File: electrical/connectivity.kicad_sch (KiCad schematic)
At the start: 0 parts

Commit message: #3 Adding controls connections to STM32, updating IOC file to match.
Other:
- company: (none) -> AlumaPower
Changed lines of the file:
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@@
 	(generator_version "9.0")
 	(paper "A4")
+	(title_block
+		(company "AlumaPower")
+	)
 	(bus_entry
 		(at 49.53 68.58)

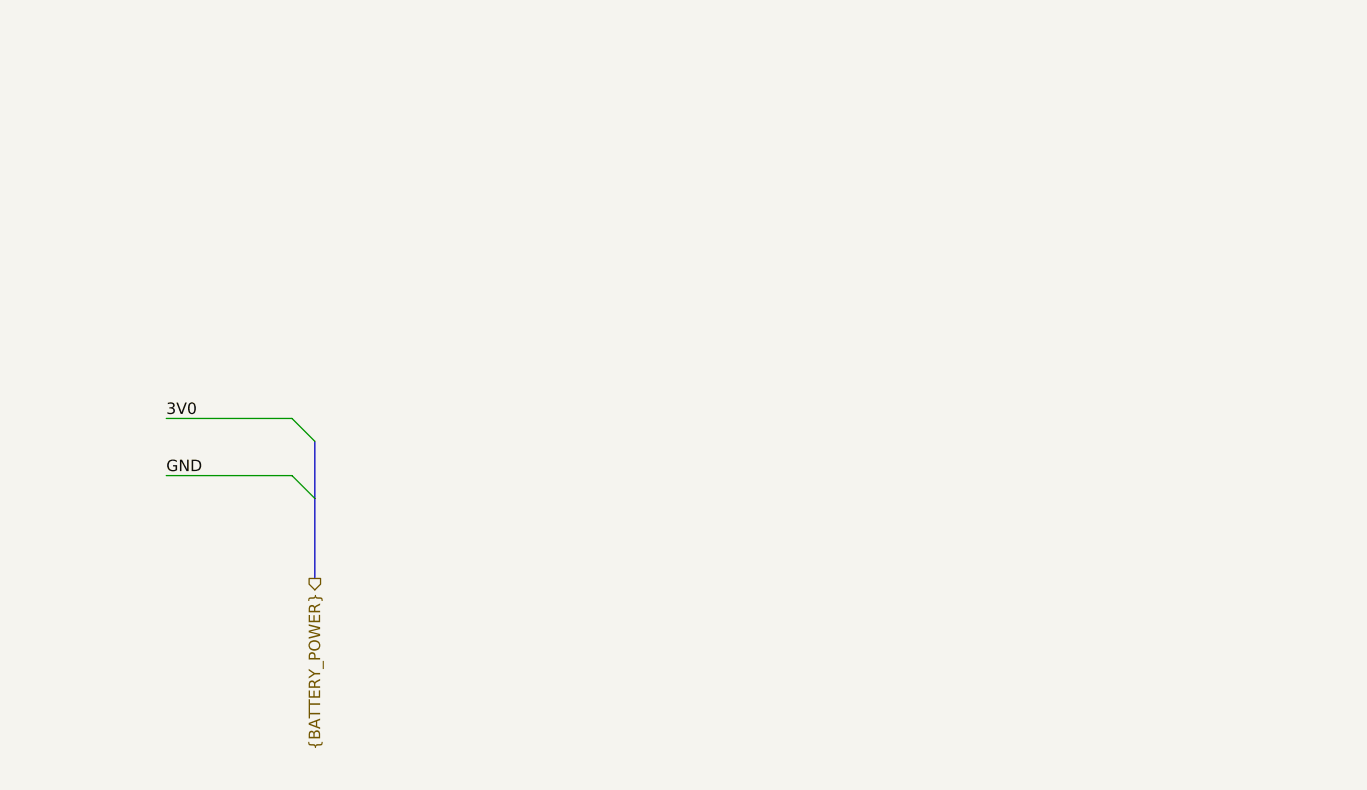
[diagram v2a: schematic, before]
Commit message: #3 Adding WiFi module to the schematic.
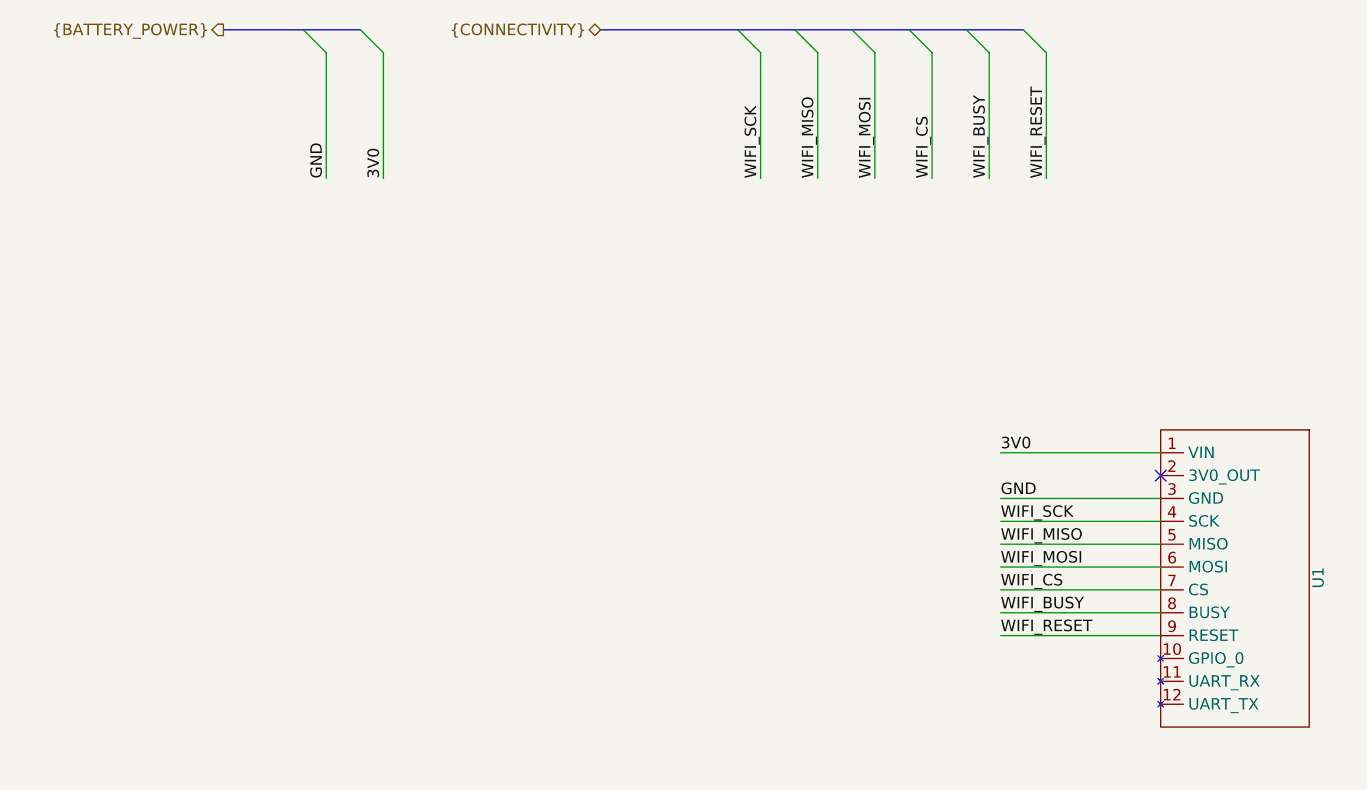
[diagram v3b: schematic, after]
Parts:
- added U1: ~, custom:esp32_wifi_module, symbol custom:wifi_module
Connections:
- net 3V0: now also U1.1 (VIN)
- net GND: now also U1.3 (GND)
- new net WIFI_BUSY: U1.8 (BUSY)
- new net WIFI_CS: U1.7 (CS)
- new net WIFI_MISO: U1.5 (MISO)
- new net WIFI_MOSI: U1.6 (MOSI)
- new net WIFI_RESET: U1.9 (RESET)
- new net WIFI_SCK: U1.4 (SCK)
- no-connect marks 0 -> 1
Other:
- title: (none) -> Etchasketch - Connectivity

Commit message: #17 Making layout. Errors rpesent.
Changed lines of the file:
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@@
 		(company "AlumaPower")
+	)
+	(bus_alias "BATTERY_POWER"
+		(members "3V0" "GND")
+	)
+	(bus_alias "CONNECTIVITY"
+		(members "WIFI_SCK" "WIFI_MISO" "WIFI_MOSI" "WIFI_CS" "WIFI_BUSY" "WIFI_RESET")
+	)
+	(bus_alias "SCREEN_INTERFACE"
+		(members "SCREEN_SDA" "SCREEN_SCL" "SCREEN_CS" "SCREEN_D_C" "SCREEN_RST"
+			"SCREEN_BUSY"
+		)
 	)
 	(no_connect
@@
 	)
 	(bus_entry
-		(at 54.61 29.21)
-		(size -2.54 -2.54)
-		(stroke
-			(width 0)
-			(type default)
-		)
-	)
-	(bus_entry
 		(at 111.76 25.4)
 		(size 2.54 2.54)
@@
 	)
 	(bus_entry
-		(at 60.96 29.21)
-		(size -2.54 -2.54)
+		(at 43.18 25.4)
+		(size 2.54 2.54)
+		(stroke
+			(width 0)
+			(type default)
+		)
+	)
+	(bus_entry
+		(at 48.26 25.4)
+		(size 2.54 2.54)
+		(stroke
+			(width 0)
+			(type default)
+		)
+	)
+	(wire
+		(pts
+			(xy 50.8 27.94) (xy 50.8 35.56)
+		)
 		(stroke
 			(width 0)
@@
 		)
 	)
+	(wire
+		(pts
+			(xy 45.72 27.94) (xy 45.72 35.56)
+		)
+		(stroke
+			(width 0)
+			(type default)
+		)
+	)
 	(bus
 		(pts
@@
 	(wire
 		(pts
-			(xy 54.61 43.18) (xy 54.61 29.21)
-		)
-		(stroke
-			(width 0)
-			(type default)
-		)
-	)
-	(wire
-		(pts
 			(xy 128.27 92.71) (xy 146.05 92.71)
 		)
@@
 	(wire
 		(pts
+			(xy 102.87 72.39) (xy 120.65 72.39)
+		)
+		(stroke
+			(width 0)
+			(type default)
+		)
+	)
+	(wire
+		(pts
 			(xy 128.27 90.17) (xy 146.05 90.17)
 		)
@@
 		)
 	)
+	(bus
+		(pts
+			(xy 40.64 25.4) (xy 43.18 25.4)
+		)
+		(stroke
+			(width 0)
+			(type default)
+		)
+	)
 	(wire
 		(pts
@@
 	(bus
 		(pts
-			(xy 52.07 26.67) (xy 43.18 26.67)
-		)
-		(stroke
-			(width 0)
-			(type default)
-		)
-	)
-	(wire
-		(pts
-			(xy 60.96 43.18) (xy 60.96 29.21)
-		)
-		(stroke
-			(width 0)
-			(type default)
-		)
-	)
-	(bus
-		(pts
 			(xy 99.06 25.4) (xy 105.41 25.4)
 		)
@@
 		)
 	)
+	(bus
+		(pts
+			(xy 43.18 25.4) (xy 48.26 25.4)
+		)
+		(stroke
+			(width 0)
+			(type default)
+		)
+	)
 	(wire
 		(pts
@@
 	(bus
 		(pts
-			(xy 58.42 26.67) (xy 52.07 26.67)
+			(xy 48.26 25.4) (xy 54.61 25.4)
 		)
 		(stroke
@@
 			(width 0)
 			(type default)
+		)
+	)
+	(label "GND"
+		(at 50.8 35.56 90)
+		(effects
+			(font
+				(size 1.27 1.27)
+			)
+			(justify left bottom)
 		)
 	)
@@
 		)
 	)
+	(label "VIN"
+		(at 120.65 72.39 180)
+		(effects
+			(font
+				(size 1.27 1.27)
+			)
+			(justify right bottom)
+		)
+	)
 	(label "WIFI_BUSY"
 		(at 120.65 41.91 90)
@@
 		)
 	)
+	(label "VIN"
+		(at 128.27 72.39 0)
+		(effects
+			(font
+				(size 1.27 1.27)
+			)
+			(justify left bottom)
+		)
+	)
 	(label "WIFI_CS"
 		(at 128.27 87.63 0)
@@
 		)
 	)
-	(label "3V0"
-		(at 128.27 72.39 0)
-		(effects
-			(font
-				(size 1.27 1.27)
-			)
-			(justify left bottom)
-		)
-	)
 	(label "WIFI_MOSI"
 		(at 128.27 85.09 0)
@@
 		)
 	)
+	(label "3V0"
+		(at 45.72 35.56 90)
+		(effects
+			(font
+				(size 1.27 1.27)
+			)
+			(justify left bottom)
+		)
+	)
 	(label "WIFI_MOSI"
 		(at 107.95 41.91 90)
@@
 		)
 	)
-	(label "3V0"
-		(at 60.96 43.18 90)
-		(effects
-			(font
-				(size 1.27 1.27)
-			)
-			(justify left bottom)
-		)
-	)
-	(label "GND"
-		(at 54.61 43.18 90)
-		(effects
-			(font
-				(size 1.27 1.27)
-			)
-			(justify left bottom)
-		)
-	)
 	(label "WIFI_CS"
 		(at 114.3 41.91 90)
@@
 		)
 	)
+	(label "3V0"
+		(at 102.87 72.39 0)
+		(effects
+			(font
+				(size 1.27 1.27)
+			)
+			(justify left bottom)
+		)
+	)
 	(label "WIFI_SCK"
 		(at 95.25 41.91 90)
@@
 	(hierarchical_label "{BATTERY_POWER}"
 		(shape passive)
-		(at 43.18 26.67 180)
-		(effects
-			(font
+		(at 40.64 25.4 180)
+		(effects
+			(font
